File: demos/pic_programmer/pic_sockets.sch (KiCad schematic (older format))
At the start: 8 parts, among them P2 SUPP28, P3 SUPP40, U1 24Cxx, U5 PIC_18_PINS, U6 PIC_8_PINS

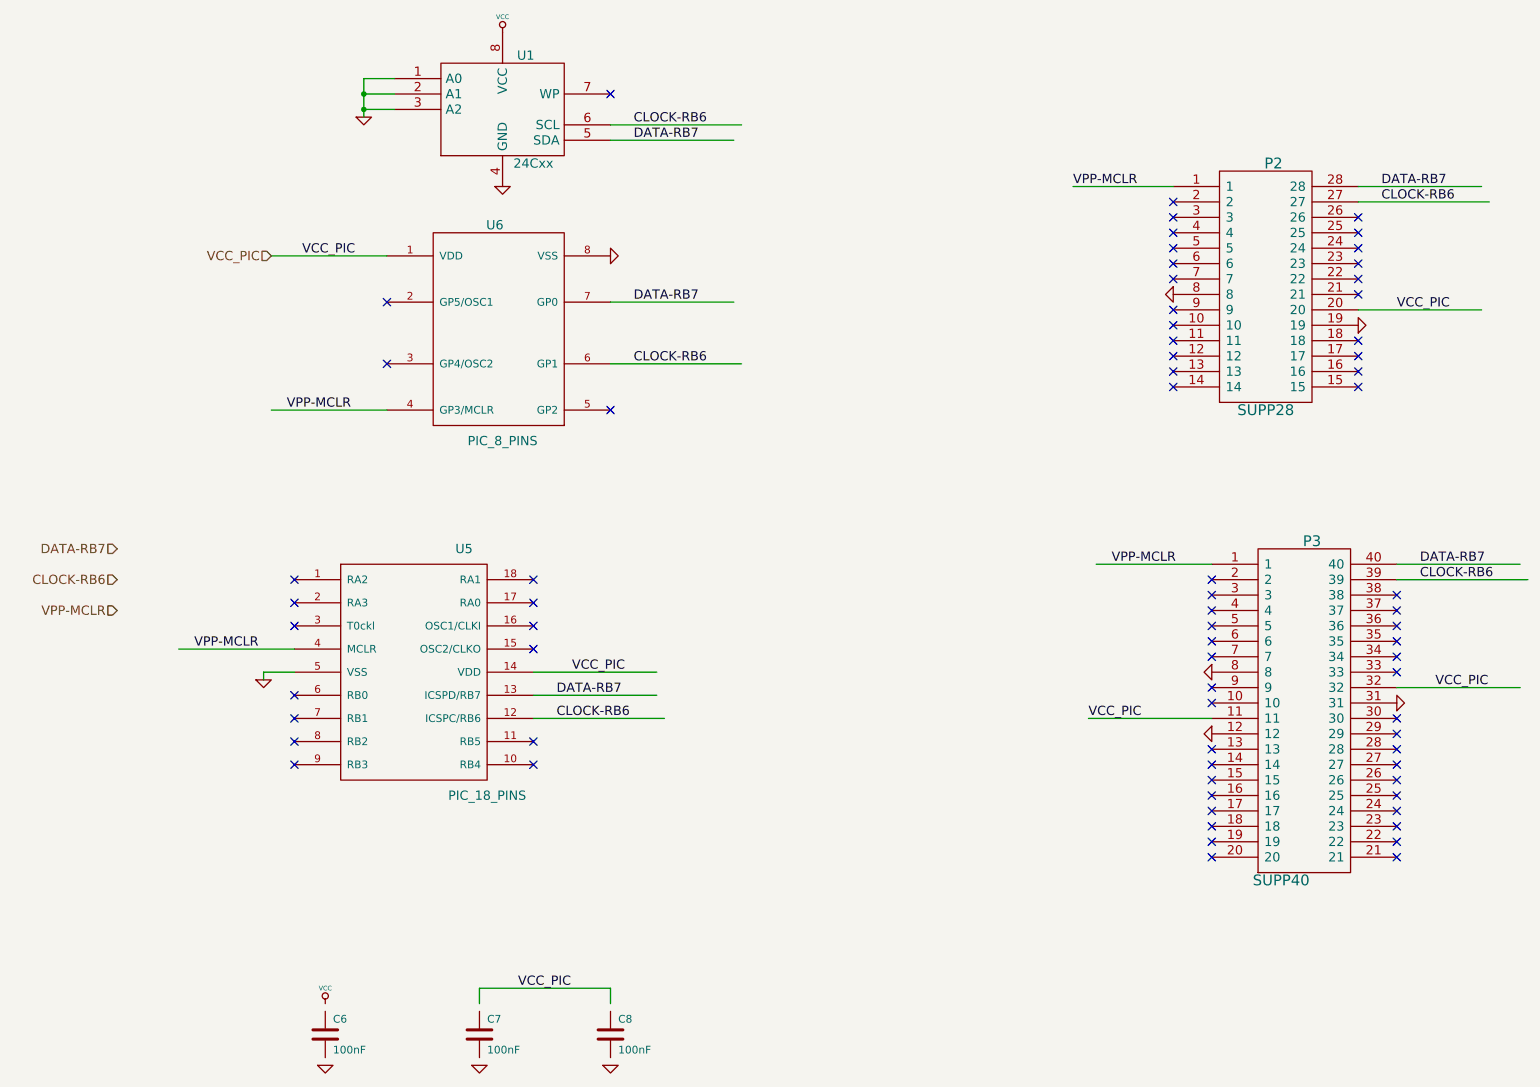
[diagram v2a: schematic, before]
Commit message: Pcbnew: Minor fix in hotkeys. Demos: add an example to use  a local fp-lib-table and local libs, and update schematics and boards.
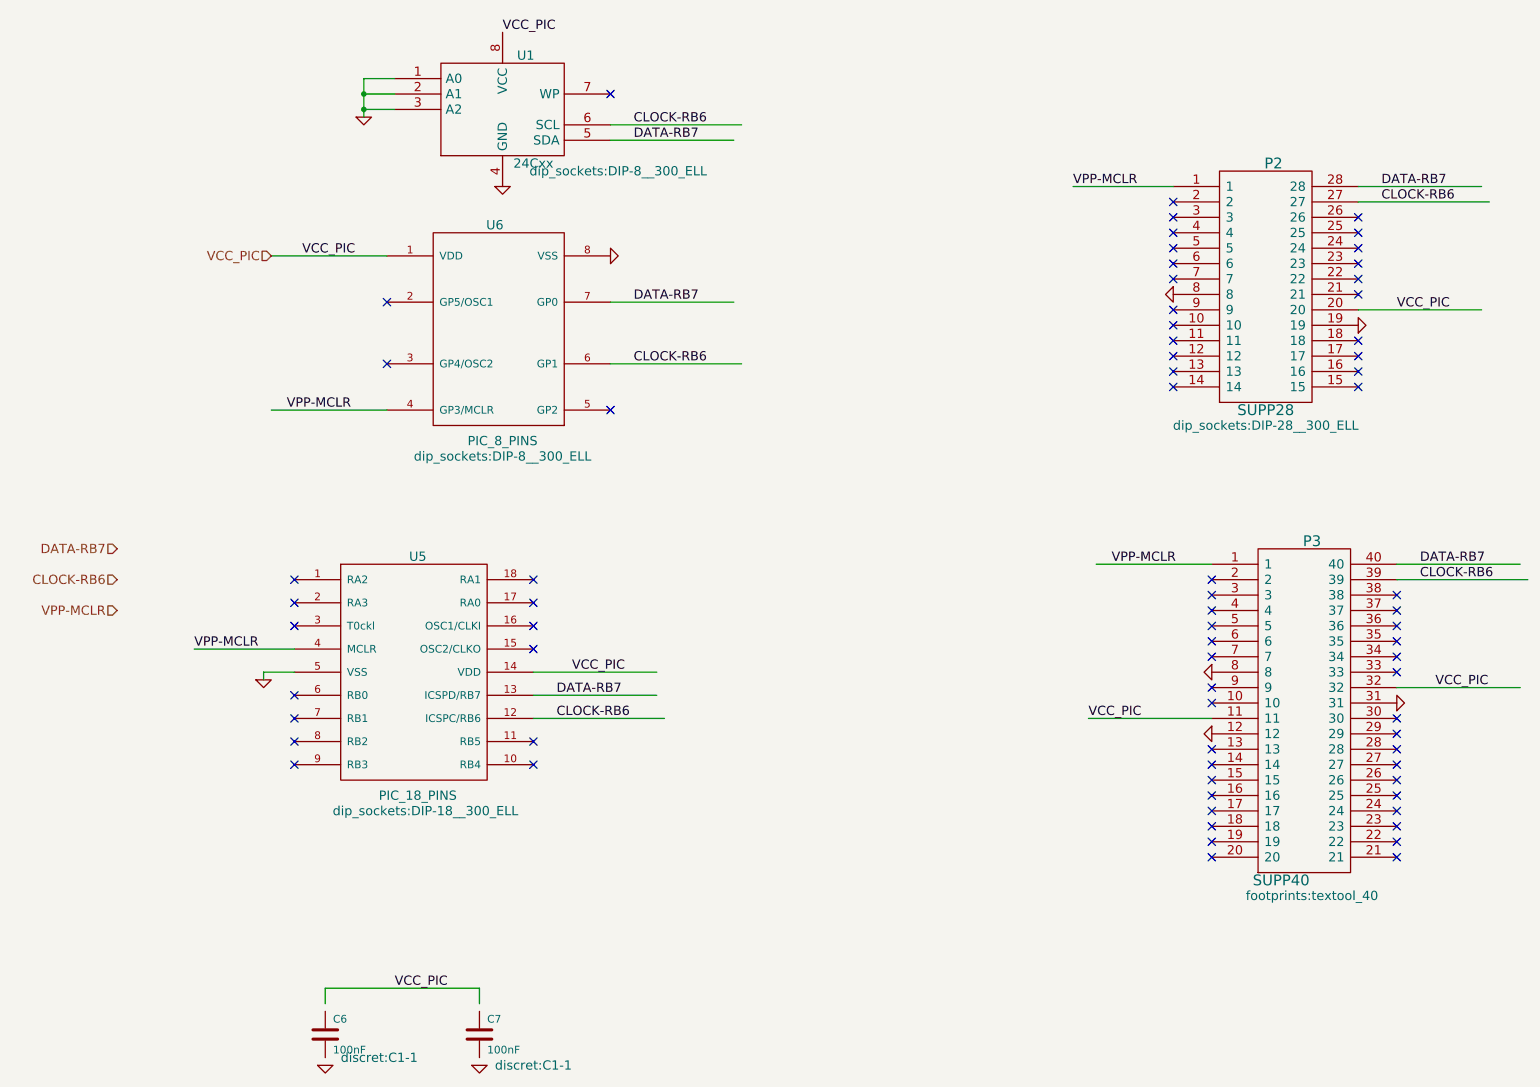
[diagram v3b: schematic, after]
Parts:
- removed C8: 100nF, symbol C
- C6, C7: footprint (none) -> discret:C1-1
- P2: footprint (none) -> dip_sockets:DIP-28__300_ELL
- P3: footprint (none) -> footprints:textool_40
- U1, U6: footprint (none) -> dip_sockets:DIP-8__300_ELL
- U5: footprint (none) -> dip_sockets:DIP-18__300_ELL
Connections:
- net labels removed: VCC
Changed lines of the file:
@@
 LIBS:power
 LIBS:device
-LIBS:transistors
+LIBS:74xx
 LIBS:conn
-LIBS:linear
-LIBS:regul
-LIBS:74xx
-LIBS:cmos4000
-LIBS:adc-dac
-LIBS:memory
 LIBS:xilinx
-LIBS:special
-LIBS:microcontrollers
-LIBS:dsp
-LIBS:microchip
-LIBS:analog_switches
-LIBS:motorola
-LIBS:texas
-LIBS:intel
-LIBS:audio
-LIBS:interface
-LIBS:digital-audio
-LIBS:philips
-LIBS:display
-LIBS:cypress
-LIBS:siliconi
-LIBS:opto
-LIBS:atmel
 LIBS:pic_programmer-cache
 EELAYER 24 0
@@
 	4050 5000 4850 5000
 Wire Wire Line
-	2500 4700 1750 4700
+	2500 4700 1850 4700
 Wire Wire Line
 	5400 2850 4550 2850
@@
 	8450 5150 7650 5150
 Wire Wire Line
-	3700 6900 4550 6900
-Wire Wire Line
-	4550 6900 4550 7000
-Text Label 3950 6900 0    60   ~ 0
+	3700 6900 2700 6900
+Text HLabel 2350 2150 0    60   Input ~ 0
+VCC_PIC
+Text Label 2550 2150 0    60   ~ 0
+VCC_PIC
+Text Label 7650 5150 0    60   ~ 0
+VCC_PIC
+Text Label 9900 4950 0    60   ~ 0
+VCC_PIC
+Text Label 9650 2500 0    60   ~ 0
 VCC_PIC
 $Comp
 L GND #PWR036
-U 1 1 4639BE2E
-P 4550 7400
-F 0 "#PWR036" H 4550 7400 30  0001 C CNN
-F 1 "GND" H 4550 7330 30  0001 C CNN
-F 2 "" H 4550 7400 60  0001 C CNN
-F 3 "" H 4550 7400 60  0001 C CNN
-	1    4550 7400
-	1    0    0    -1
-$EndComp
-$Comp
-L C C8
-U 1 1 4639BE2C
-P 4550 7200
-F 0 "C8" H 4600 7300 50  0000 L CNN
-F 1 "100nF" H 4600 7100 50  0000 L CNN
-F 2 "" H 4550 7200 60  0001 C CNN
-F 3 "" H 4550 7200 60  0001 C CNN
-	1    4550 7200
-	1    0    0    -1
-$EndComp
-Text HLabel 2350 2150 0    60   Input ~ 0
-VCC_PIC
-Text Label 2550 2150 0    60   ~ 0
-VCC_PIC
-Text Label 7650 5150 0    60   ~ 0
-VCC_PIC
-Text Label 9900 4950 0    60   ~ 0
-VCC_PIC
-Text Label 9650 2500 0    60   ~ 0
-VCC_PIC
-$Comp
-L GND #PWR037
 U 1 1 442A8794
 P 8450 5250
-F 0 "#PWR037" H 8450 5250 30  0001 C CNN
+F 0 "#PWR036" H 8450 5250 30  0001 C CNN
 F 1 "GND" H 8450 5180 30  0001 C CNN
 F 2 "" H 8450 5250 60  0001 C CNN
@@
 VCC_PIC
 $Comp
-L GND #PWR038
+L GND #PWR037
 U 1 1 443CCA5D
 P 8450 4850
-F 0 "#PWR038" H 8450 4850 30  0001 C CNN
+F 0 "#PWR037" H 8450 4850 30  0001 C CNN
 F 1 "GND" H 8450 4780 30  0001 C CNN
 F 2 "" H 8450 4850 60  0001 C CNN
@@
 NoConn ~ 8200 1800
 $Comp
-L GND #PWR039
+L GND #PWR038
 U 1 1 443697C7
 P 9400 2600
-F 0 "#PWR039" H 9400 2600 30  0001 C CNN
+F 0 "#PWR038" H 9400 2600 30  0001 C CNN
 F 1 "GND" H 9400 2530 30  0001 C CNN
 F 2 "" H 9400 2600 60  0001 C CNN
@@
 $EndComp
 $Comp
-L GND #PWR040
+L GND #PWR039
 U 1 1 443697C3
 P 8200 2400
-F 0 "#PWR040" H 8200 2400 30  0001 C CNN
+F 0 "#PWR039" H 8200 2400 30  0001 C CNN
 F 1 "GND" H 8200 2330 30  0001 C CNN
 F 2 "" H 8200 2400 60  0001 C CNN
@@
 F 0 "P2" H 8850 3150 70  0000 C CNN
 F 1 "SUPP28" H 8800 1550 70  0000 C CNN
-F 2 "" H 8800 2350 60  0001 C CNN
+F 2 "dip_sockets:DIP-28__300_ELL" H 8800 1450 60  0000 C CNN
 F 3 "" H 8800 2350 60  0001 C CNN
 	1    8800 2350
@@
 $EndComp
 $Comp
-L GND #PWR041
+L GND #PWR040
 U 1 1 442AA147
 P 3700 7400
-F 0 "#PWR041" H 3700 7400 30  0001 C CNN
+F 0 "#PWR040" H 3700 7400 30  0001 C CNN
 F 1 "GND" H 3700 7330 30  0001 C CNN
 F 2 "" H 3700 7400 60  0001 C CNN
@@
 F 0 "C7" H 3750 7300 50  0000 L CNN
 F 1 "100nF" H 3750 7100 50  0000 L CNN
-F 2 "" H 3700 7200 60  0001 C CNN
+F 2 "discret:C1-1" H 4050 7000 60  0000 C CNN
 F 3 "" H 3700 7200 60  0001 C CNN
 	1    3700 7200
@@
 $EndComp
 $Comp
-L GND #PWR042
+L GND #PWR041
 U 1 1 442AA138
 P 2700 7400
-F 0 "#PWR042" H 2700 7400 30  0001 C CNN
+F 0 "#PWR041" H 2700 7400 30  0001 C CNN
 F 1 "GND" H 2700 7330 30  0001 C CNN
 F 2 "" H 2700 7400 60  0001 C CNN
 F 3 "" H 2700 7400 60  0001 C CNN
 	1    2700 7400
-	1    0    0    -1
-$EndComp
-$Comp
-L VCC #PWR043
-U 1 1 442AA134
-P 2700 7000
-F 0 "#PWR043" H 2700 7100 30  0001 C CNN
-F 1 "VCC" H 2700 7100 30  0000 C CNN
-F 2 "" H 2700 7000 60  0001 C CNN
-F 3 "" H 2700 7000 60  0001 C CNN
-	1    2700 7000
-	1    0    0    -1
-$EndComp
-$Comp
-L C C6
-U 1 1 442AA12B
-P 2700 7200
-F 0 "C6" H 2750 7300 50  0000 L CNN
-F 1 "100nF" H 2750 7100 50  0000 L CNN
-F 2 "" H 2700 7200 60  0001 C CNN
-F 3 "" H 2700 7200 60  0001 C CNN
-	1    2700 7200
 	1    0    0    -1
 $EndComp
@@
 NoConn ~ 8450 4250
 $Comp
-L GND #PWR044
+L GND #PWR042
 U 1 1 442A896A
 P 9650 5050
-F 0 "#PWR044" H 9650 5050 30  0001 C CNN
+F 0 "#PWR042" H 9650 5050 30  0001 C CNN
 F 1 "GND" H 9650 4980 30  0001 C CNN
 F 2 "" H 9650 5050 60  0001 C CNN
@@
 F 0 "P3" H 9100 6200 70  0000 C CNN
 F 1 "SUPP40" H 8900 4000 70  0000 C CNN
-F 2 "" H 9050 5100 60  0001 C CNN
+F 2 "footprints:textool_40" H 9100 3900 60  0000 C CNN
 F 3 "" H 9050 5100 60  0001 C CNN
 	1    9050 5100
@@
 NoConn ~ 4550 1100
 $Comp
-L GND #PWR045
+L GND #PWR043
 U 1 1 442A8838
 P 2950 1250
-F 0 "#PWR045" H 2950 1250 30  0001 C CNN
+F 0 "#PWR043" H 2950 1250 30  0001 C CNN
 F 1 "GND" H 2950 1180 30  0001 C CNN
 F 2 "" H 2950 1250 60  0001 C CNN
@@
 F 0 "U1" H 4000 1550 60  0000 C CNN
 F 1 "24Cxx" H 4050 850 60  0000 C CNN
-F 2 "" H 3850 1200 60  0001 C CNN
+F 2 "dip_sockets:DIP-8__300_ELL" H 4600 800 60  0000 C CNN
 F 3 "" H 3850 1200 60  0001 C CNN
 	1    3850 1200
@@
 U 1 1 442A81A7
 P 3300 4850
-F 0 "U5" H 3600 5650 60  0000 C CNN
-F 1 "PIC_18_PINS" H 3750 4050 60  0000 C CNN
-F 2 "" H 3300 4850 60  0001 C CNN
+F 0 "U5" H 3300 5600 60  0000 C CNN
+F 1 "PIC_18_PINS" H 3300 4050 60  0000 C CNN
+F 2 "dip_sockets:DIP-18__300_ELL" H 3350 3950 60  0000 C CNN
 F 3 "" H 3300 4850 60  0001 C CNN
 	1    3300 4850
@@
 DATA-RB7
 $Comp
-L GND #PWR046
+L GND #PWR044
 U 1 1 442A820F
 P 2300 4900
-F 0 "#PWR046" H 2300 4900 30  0001 C CNN
+F 0 "#PWR044" H 2300 4900 30  0001 C CNN
 F 1 "GND" H 2300 4830 30  0001 C CNN
 F 2 "" H 2300 4900 60  0001 C CNN
@@
 $EndComp
 $Comp
-L GND #PWR047
+L GND #PWR045
 U 1 1 442A8205
 P 4550 2150
-F 0 "#PWR047" H 4550 2150 30  0001 C CNN
+F 0 "#PWR045" H 4550 2150 30  0001 C CNN
 F 1 "GND" H 4550 2080 30  0001 C CNN
 F 2 "" H 4550 2150 60  0001 C CNN
@@
 F 0 "U6" H 3800 3350 60  0000 C CNN
 F 1 "PIC_8_PINS" H 3850 1950 60  0000 C CNN
-F 2 "" H 3850 2650 60  0001 C CNN
+F 2 "dip_sockets:DIP-8__300_ELL" H 3850 1850 60  0000 C CNN
 F 3 "" H 3850 2650 60  0001 C CNN
 	1    3850 2650
@@
 $EndComp
 $Comp
-L GND #PWR048
+L GND #PWR046
 U 1 1 52C92629
 P 3850 1700
-F 0 "#PWR048" H 3850 1700 30  0001 C CNN
+F 0 "#PWR046" H 3850 1700 30  0001 C CNN
 F 1 "GND" H 3850 1630 30  0001 C CNN
 F 2 "" H 3850 1700 60  0001 C CNN
@@
 	1    0    0    -1
 $EndComp
-$Comp
-L VCC #PWR049
-U 1 1 52C92634
-P 3850 700
-F 0 "#PWR049" H 3850 800 30  0001 C CNN
-F 1 "VCC" H 3850 800 30  0000 C CNN
-F 2 "" H 3850 700 60  0001 C CNN
-F 3 "" H 3850 700 60  0001 C CNN
-	1    3850 700
-	1    0    0    -1
-$EndComp
+Text Label 3850 700  0    60   ~ 0
+VCC_PIC
+$Comp
+L C C6
+U 1 1 442AA12B
+P 2700 7200
+F 0 "C6" H 2750 7300 50  0000 L CNN
+F 1 "100nF" H 2750 7100 50  0000 L CNN
+F 2 "discret:C1-1" H 3050 7050 60  0000 C CNN
+F 3 "" H 2700 7200 60  0001 C CNN
+	1    2700 7200
+	1    0    0    -1
+$EndComp
+Wire Wire Line
+	2700 6900 2700 7000
+Text Label 3150 6900 0    60   ~ 0
+VCC_PIC
 $EndSCHEMATC

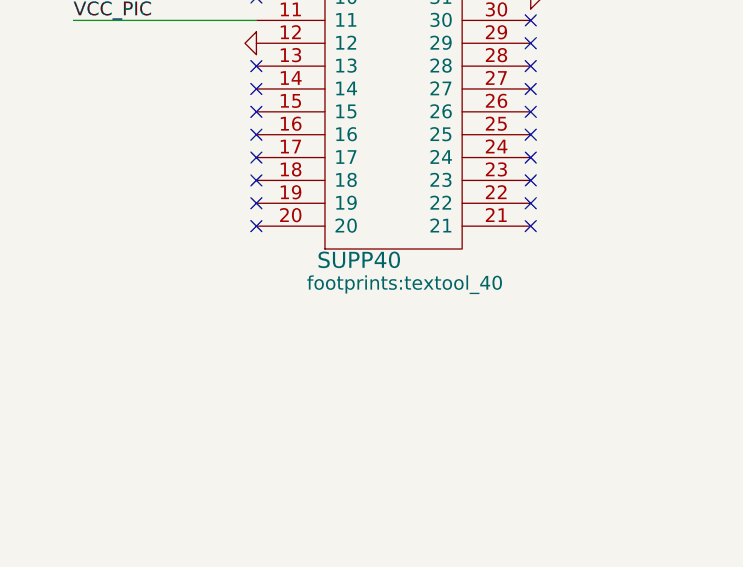
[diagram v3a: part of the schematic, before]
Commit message: Minor fixes: specctra export: skip malformed circles (having a radius = 0)  in board outline creation, which can crash 3d-viewer or vrml export. dialog_fp_lib_table: remember during a session the last open table (global or local). drawing_tool: fix compil warning Update demos.
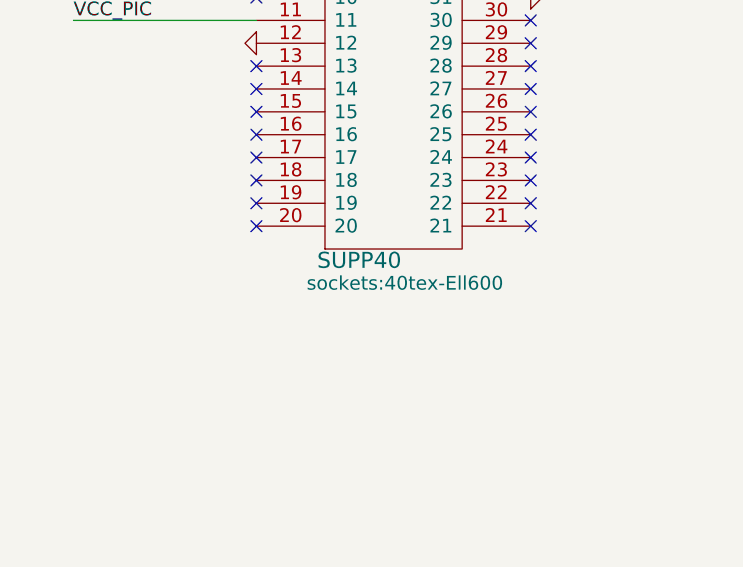
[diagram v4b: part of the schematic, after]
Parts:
- P3: footprint footprints:textool_40 -> sockets:40tex-Ell600
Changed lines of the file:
@@
 F 0 "P3" H 9100 6200 70  0000 C CNN
 F 1 "SUPP40" H 8900 4000 70  0000 C CNN
-F 2 "footprints:textool_40" H 9100 3900 60  0000 C CNN
+F 2 "sockets:40tex-Ell600" H 9100 3900 60  0000 C CNN
 F 3 "" H 9050 5100 60  0001 C CNN
 	1    9050 5100
